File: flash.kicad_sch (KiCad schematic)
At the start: 2 parts

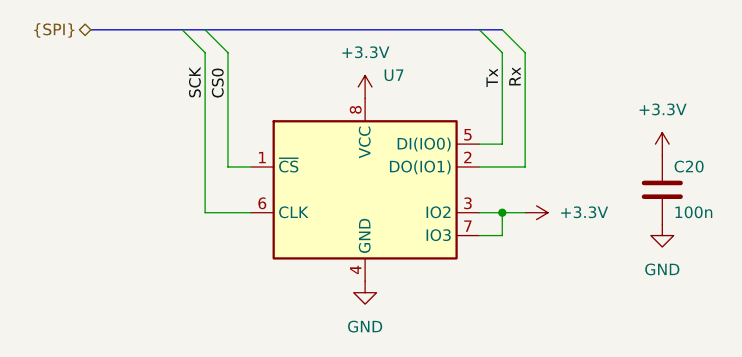
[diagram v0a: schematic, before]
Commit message: Geographical reannotated
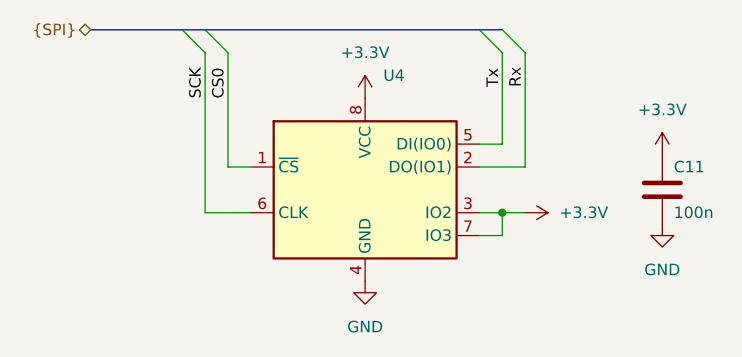
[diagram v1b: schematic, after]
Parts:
- renumbered C20 to C11, U7 to U4
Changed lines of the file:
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@@
   (symbol (lib_id "Device:C") (at 87.63 39.37 0) (unit 1)
     (in_bom yes) (on_board yes)
-    (property "Reference" "C20" (id 0) (at 88.9 36.83 0)
+    (property "Reference" "C11" (id 0) (at 88.9 36.83 0)
       (effects (font (size 1.27 1.27)) (justify left))
     )
@@
   (symbol (lib_id "Memory_Flash:W25Q32JVSS") (at 54.61 39.37 0) (unit 1)
     (in_bom yes) (on_board yes) (fields_autoplaced)
-    (property "Reference" "U7" (id 0) (at 56.6294 26.67 0)
+    (property "Reference" "U4" (id 0) (at 56.6294 26.67 0)
       (effects (font (size 1.27 1.27)) (justify left))
     )

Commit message: Final refinements before issue to JLC
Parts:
- renumbered C11 to C20, U4 to U7
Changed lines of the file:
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@@
   (symbol (lib_id "power:+3.3V") (at 72.39 41.91 270) (unit 1)
     (in_bom yes) (on_board yes) (fields_autoplaced)
-    (property "Reference" "#PWR044" (id 0) (at 68.58 41.91 0)
+    (property "Reference" "#PWR046" (id 0) (at 68.58 41.91 0)
       (effects (font (size 1.27 1.27)) hide)
     )
@@
   (symbol (lib_id "power:GND") (at 54.61 49.53 0) (unit 1)
     (in_bom yes) (on_board yes) (fields_autoplaced)
-    (property "Reference" "#PWR043" (id 0) (at 54.61 55.88 0)
+    (property "Reference" "#PWR045" (id 0) (at 54.61 55.88 0)
       (effects (font (size 1.27 1.27)) hide)
     )
@@
   (symbol (lib_id "power:+3.3V") (at 87.63 35.56 0) (unit 1)
     (in_bom yes) (on_board yes) (fields_autoplaced)
-    (property "Reference" "#PWR045" (id 0) (at 87.63 39.37 0)
+    (property "Reference" "#PWR047" (id 0) (at 87.63 39.37 0)
       (effects (font (size 1.27 1.27)) hide)
     )
@@
   (symbol (lib_id "Device:C") (at 87.63 39.37 0) (unit 1)
     (in_bom yes) (on_board yes)
-    (property "Reference" "C11" (id 0) (at 88.9 36.83 0)
+    (property "Reference" "C20" (id 0) (at 88.9 36.83 0)
       (effects (font (size 1.27 1.27)) (justify left))
     )
@@
   (symbol (lib_id "Memory_Flash:W25Q32JVSS") (at 54.61 39.37 0) (unit 1)
     (in_bom yes) (on_board yes) (fields_autoplaced)
-    (property "Reference" "U4" (id 0) (at 56.6294 26.67 0)
+    (property "Reference" "U7" (id 0) (at 56.6294 26.67 0)
       (effects (font (size 1.27 1.27)) (justify left))
     )
@@
   (symbol (lib_id "power:GND") (at 87.63 43.18 0) (unit 1)
     (in_bom yes) (on_board yes) (fields_autoplaced)
-    (property "Reference" "#PWR046" (id 0) (at 87.63 49.53 0)
+    (property "Reference" "#PWR048" (id 0) (at 87.63 49.53 0)
       (effects (font (size 1.27 1.27)) hide)
     )
@@
   (symbol (lib_id "power:+3.3V") (at 54.61 29.21 0) (unit 1)
     (in_bom yes) (on_board yes) (fields_autoplaced)
-    (property "Reference" "#PWR042" (id 0) (at 54.61 33.02 0)
+    (property "Reference" "#PWR044" (id 0) (at 54.61 33.02 0)
       (effects (font (size 1.27 1.27)) hide)
     )
